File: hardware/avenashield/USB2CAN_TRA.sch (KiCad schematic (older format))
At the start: 29 parts, among them U4 STM32F042C6Tx, U5 MCP2551-I-SN, U9 TXS0102DCT, Y2 16 MHz

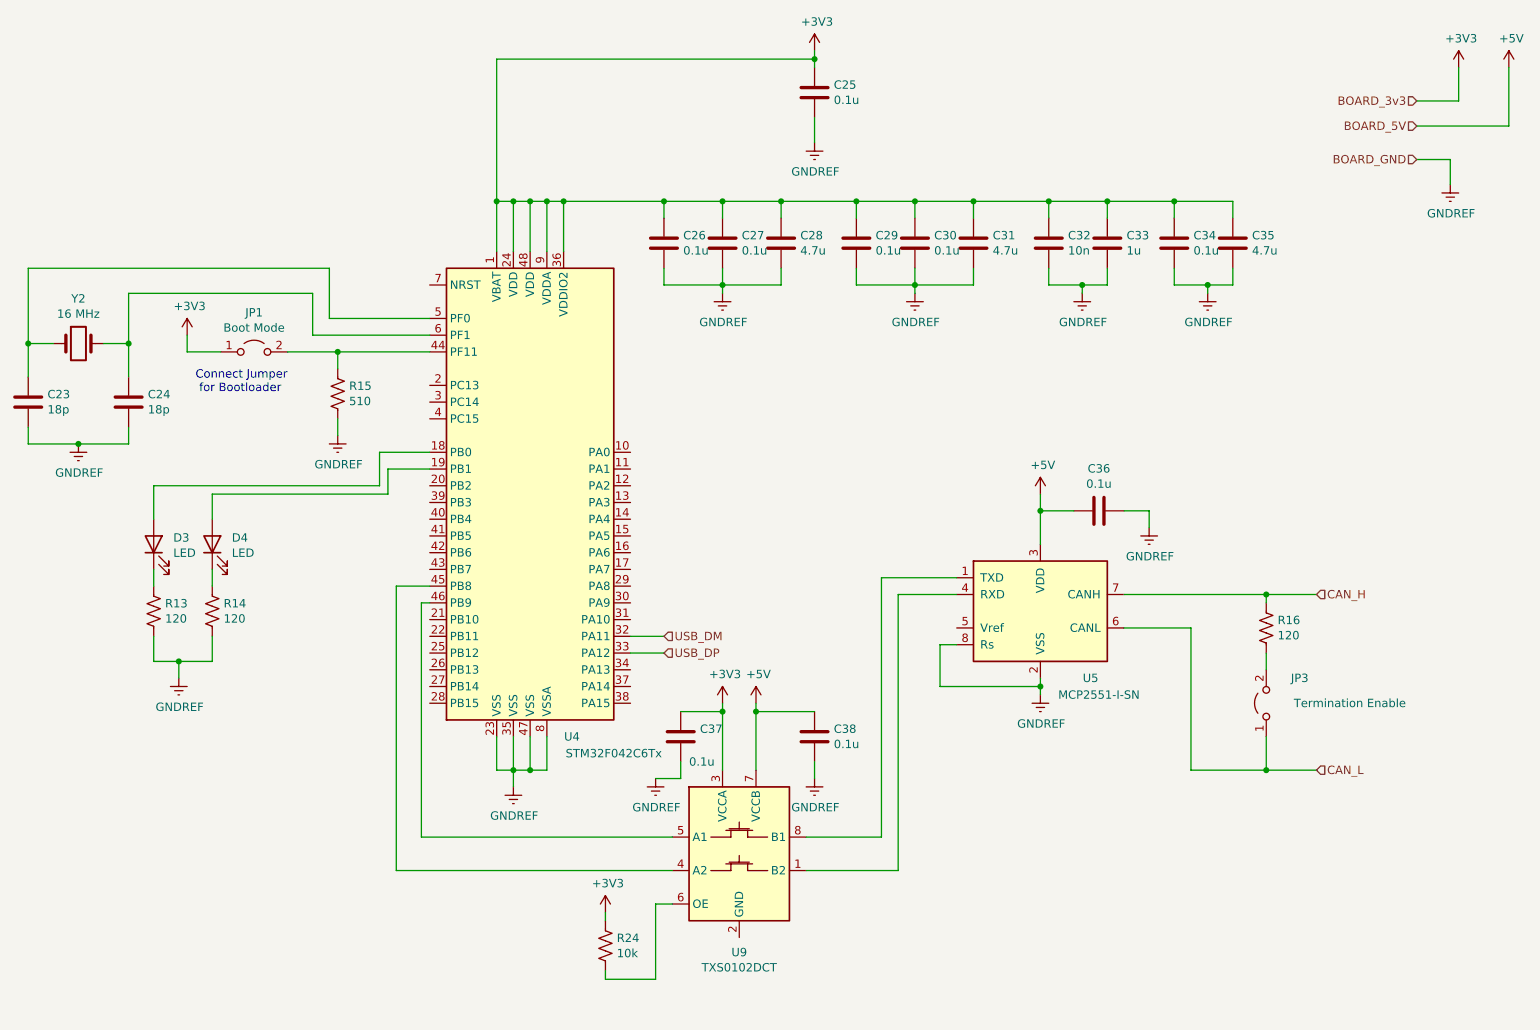
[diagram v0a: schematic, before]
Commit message: Added MiniPCIe latch clip and replaced onboard LEDs with connector
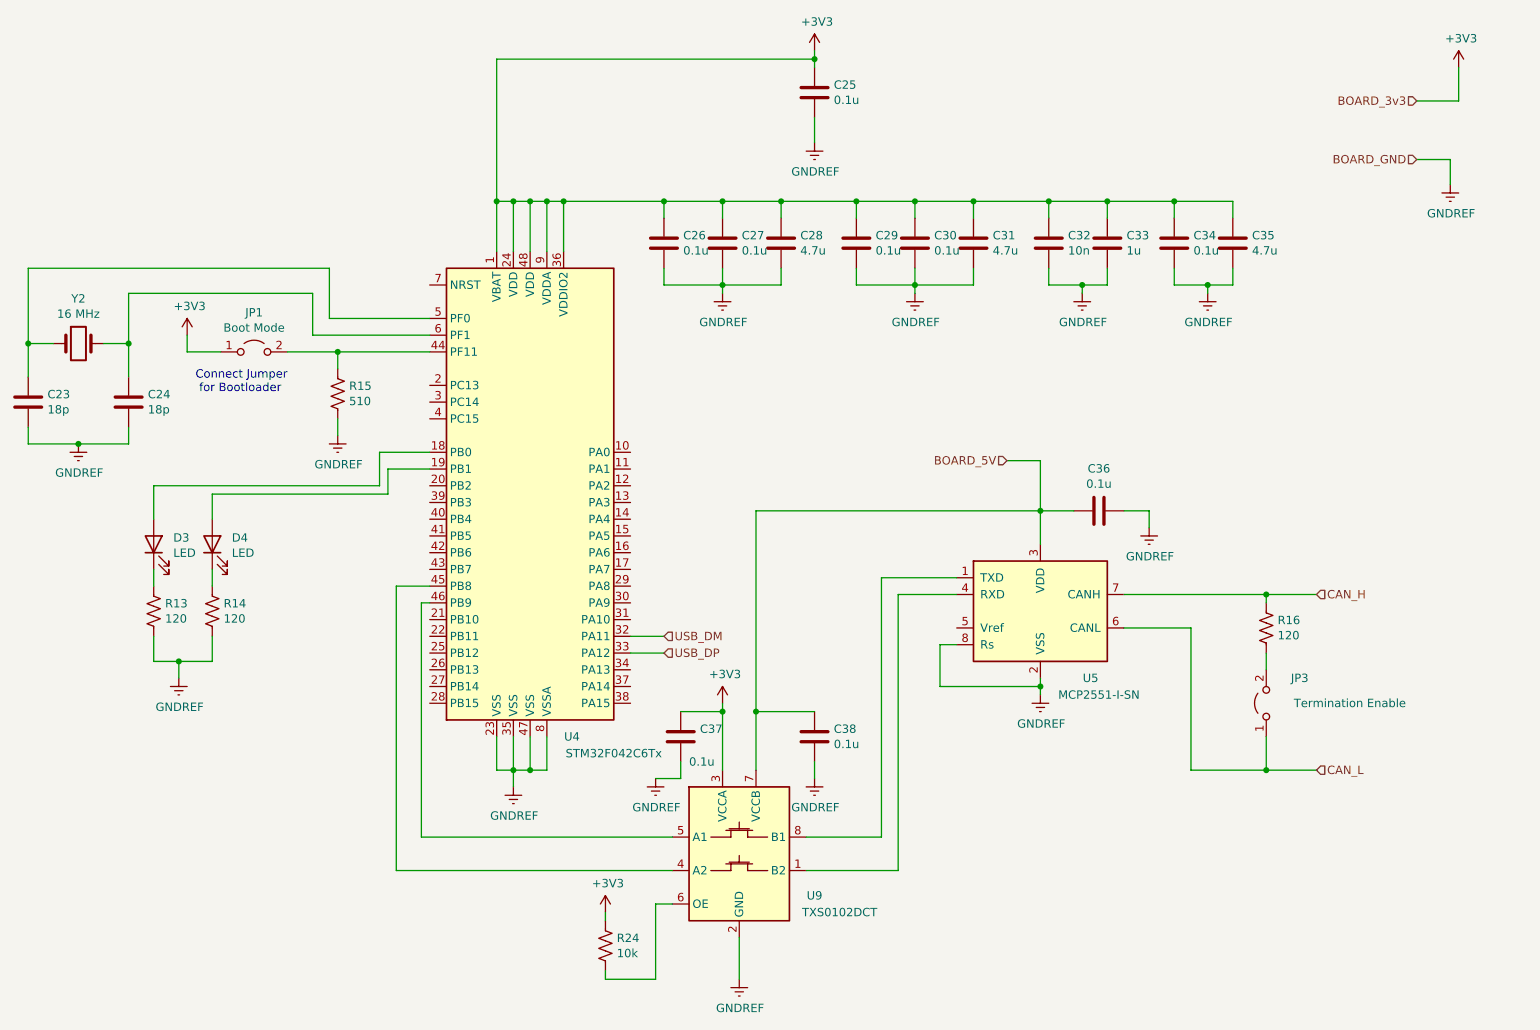
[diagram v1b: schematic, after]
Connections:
- net GNDREF: now also U9.2 (GND)
- net +5V renamed BOARD_5V
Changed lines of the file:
@@
 $EndComp
-$Comp
-L power:+5V #PWR0153
-U 1 1 5E591CA5
-P 7400 3450
-AR Path="/5E564EEA/5E591CA5" Ref="#PWR0153"  Part="1"
-AR Path="/5E45C906/5E591CA5" Ref="#PWR?"  Part="1"
-F 0 "#PWR0153" H 7400 3300 50  0001 C CNN
-F 1 "+5V" H 7415 3623 50  0000 C CNN
-F 2 "" H 7400 3450 50  0001 C CNN
-F 3 "" H 7400 3450 50  0001 C CNN
-	1    7400 3450
-	1    0    0    -1
-$EndComp
-Wire Wire Line
-	7400 3450 7400 3550
 $Comp
 L power:GNDREF #PWR0154
@@
 	1    0    0    -1
 $EndComp
-$Comp
-L power:+5V #PWR0162
-U 1 1 5E61AB69
-P 10200 900
-AR Path="/5E564EEA/5E61AB69" Ref="#PWR0162"  Part="1"
-AR Path="/5E45C906/5E61AB69" Ref="#PWR?"  Part="1"
-F 0 "#PWR0162" H 10200 750 50  0001 C CNN
-F 1 "+5V" H 10215 1073 50  0000 C CNN
-F 2 "" H 10200 900 50  0001 C CNN
-F 3 "" H 10200 900 50  0001 C CNN
-	1    10200 900
-	1    0    0    -1
-$EndComp
 Text HLabel 9650 1100 0    50   Input ~ 0
 BOARD_3v3
-Text HLabel 9650 1250 0    50   Input ~ 0
+Text HLabel 7200 3250 0    50   Input ~ 0
 BOARD_5V
 Wire Wire Line
@@
 Wire Wire Line
 	9900 1100 9900 900
-Wire Wire Line
-	10200 900  10200 1250
-Wire Wire Line
-	10200 1250 9650 1250
 Text HLabel 9650 1450 0    50   Input ~ 0
 BOARD_GND
@@
 U 1 1 5E61F145
 P 5600 5600
-F 0 "U9" H 5600 5011 50  0000 C CNN
-F 1 "TXS0102DCT" H 5600 4920 50  0000 C CNN
+F 0 "U9" H 6050 5350 50  0000 C CNN
+F 1 "TXS0102DCT" H 6200 5250 50  0000 C CNN
 F 2 "Package_SO:SSOP-8_2.95x2.8mm_P0.65mm" H 5600 5050 50  0001 C CNN
 F 3 "http://www.ti.com/lit/gpn/txs0102" H 5600 5580 50  0001 C CNN
@@
 Wire Wire Line
 	3550 4000 3550 5700
-$Comp
-L power:+5V #PWR0140
-U 1 1 5E63CF51
-P 5700 4700
-F 0 "#PWR0140" H 5700 4550 50  0001 C CNN
-F 1 "+5V" H 5715 4873 50  0000 C CNN
-F 2 "" H 5700 4700 50  0001 C CNN
-F 3 "" H 5700 4700 50  0001 C CNN
-	1    5700 4700
-	1    0    0    -1
-$EndComp
 $Comp
 L power:+3V3 #PWR0184
@@
 	1    0    0    -1
 $EndComp
-Wire Wire Line
-	5700 4700 5700 4750
 Wire Wire Line
 	5500 4700 5500 4750
@@
 Wire Wire Line
 	5100 5900 5200 5900
+$Comp
+L power:GNDREF #PWR0195
+U 1 1 5E715CCE
+P 5600 6350
+AR Path="/5E564EEA/5E715CCE" Ref="#PWR0195"  Part="1"
+AR Path="/5E45C906/5E715CCE" Ref="#PWR?"  Part="1"
+F 0 "#PWR0195" H 5600 6100 50  0001 C CNN
+F 1 "GNDREF" H 5605 6177 50  0000 C CNN
+F 2 "" H 5600 6350 50  0001 C CNN
+F 3 "" H 5600 6350 50  0001 C CNN
+	1    5600 6350
+	1    0    0    -1
+$EndComp
+Wire Wire Line
+	5600 6350 5600 6100
+Wire Wire Line
+	7200 3250 7400 3250
+Wire Wire Line
+	7400 3250 7400 3550
+Wire Wire Line
+	5700 3550 7400 3550
+Wire Wire Line
+	5700 3550 5700 4750
 $EndSCHEMATC

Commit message: Changed footprints for CAN connectors and replaced 3D models for headers
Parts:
- C23, C24, C25, C26, C27, C28, C29, C30, C31, C32, C33, C34, C35, C36, C37, C38: footprint Capacitor_SMD:C_0603_1608Metric -> Capacitor_SMD:C_0805_2012Metric_Pad1.15x1.40mm_HandSolder
- R13, R14, R15, R16, R24: footprint Resistor_SMD:R_1206_3216Metric -> Resistor_SMD:R_0805_2012Metric_Pad1.15x1.40mm_HandSolder
- Y2: footprint Crystal:Crystal_SMD_2016-4Pin_2.0x1.6mm -> Crystal:Crystal_SMD_HC49-SD
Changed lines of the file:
@@
 F 0 "C25" H 6165 1096 50  0000 L CNN
 F 1 "0.1u" H 6165 1005 50  0000 L CNN
-F 2 "Capacitor_SMD:C_0603_1608Metric" H 6088 900 50  0001 C CNN
+F 2 "Capacitor_SMD:C_0805_2012Metric_Pad1.15x1.40mm_HandSolder" H 6088 900 50  0001 C CNN
 F 3 "~" H 6050 1050 50  0001 C CNN
 	1    6050 1050
@@
 F 0 "C26" H 5265 1996 50  0000 L CNN
 F 1 "0.1u" H 5265 1905 50  0000 L CNN
-F 2 "Capacitor_SMD:C_0603_1608Metric" H 5188 1800 50  0001 C CNN
+F 2 "Capacitor_SMD:C_0805_2012Metric_Pad1.15x1.40mm_HandSolder" H 5188 1800 50  0001 C CNN
 F 3 "~" H 5150 1950 50  0001 C CNN
 	1    5150 1950
@@
 F 0 "C27" H 5615 1996 50  0000 L CNN
 F 1 "0.1u" H 5615 1905 50  0000 L CNN
-F 2 "Capacitor_SMD:C_0603_1608Metric" H 5538 1800 50  0001 C CNN
+F 2 "Capacitor_SMD:C_0805_2012Metric_Pad1.15x1.40mm_HandSolder" H 5538 1800 50  0001 C CNN
 F 3 "~" H 5500 1950 50  0001 C CNN
 	1    5500 1950
@@
 F 0 "C28" H 5965 1996 50  0000 L CNN
 F 1 "4.7u" H 5965 1905 50  0000 L CNN
-F 2 "Capacitor_SMD:C_0603_1608Metric" H 5888 1800 50  0001 C CNN
+F 2 "Capacitor_SMD:C_0805_2012Metric_Pad1.15x1.40mm_HandSolder" H 5888 1800 50  0001 C CNN
 F 3 "~" H 5850 1950 50  0001 C CNN
 	1    5850 1950
@@
 F 0 "C29" H 6415 1996 50  0000 L CNN
 F 1 "0.1u" H 6415 1905 50  0000 L CNN
-F 2 "Capacitor_SMD:C_0603_1608Metric" H 6338 1800 50  0001 C CNN
+F 2 "Capacitor_SMD:C_0805_2012Metric_Pad1.15x1.40mm_HandSolder" H 6338 1800 50  0001 C CNN
 F 3 "~" H 6300 1950 50  0001 C CNN
 	1    6300 1950
@@
 F 0 "C30" H 6765 1996 50  0000 L CNN
 F 1 "0.1u" H 6765 1905 50  0000 L CNN
-F 2 "Capacitor_SMD:C_0603_1608Metric" H 6688 1800 50  0001 C CNN
+F 2 "Capacitor_SMD:C_0805_2012Metric_Pad1.15x1.40mm_HandSolder" H 6688 1800 50  0001 C CNN
 F 3 "~" H 6650 1950 50  0001 C CNN
 	1    6650 1950
@@
 F 0 "C31" H 7115 1996 50  0000 L CNN
 F 1 "4.7u" H 7115 1905 50  0000 L CNN
-F 2 "Capacitor_SMD:C_0603_1608Metric" H 7038 1800 50  0001 C CNN
+F 2 "Capacitor_SMD:C_0805_2012Metric_Pad1.15x1.40mm_HandSolder" H 7038 1800 50  0001 C CNN
 F 3 "~" H 7000 1950 50  0001 C CNN
 	1    7000 1950
@@
 F 0 "C32" H 7565 1996 50  0000 L CNN
 F 1 "10n" H 7565 1905 50  0000 L CNN
-F 2 "Capacitor_SMD:C_0603_1608Metric" H 7488 1800 50  0001 C CNN
+F 2 "Capacitor_SMD:C_0805_2012Metric_Pad1.15x1.40mm_HandSolder" H 7488 1800 50  0001 C CNN
 F 3 "~" H 7450 1950 50  0001 C CNN
 	1    7450 1950
@@
 F 0 "C33" H 7915 1996 50  0000 L CNN
 F 1 "1u" H 7915 1905 50  0000 L CNN
-F 2 "Capacitor_SMD:C_0603_1608Metric" H 7838 1800 50  0001 C CNN
+F 2 "Capacitor_SMD:C_0805_2012Metric_Pad1.15x1.40mm_HandSolder" H 7838 1800 50  0001 C CNN
 F 3 "~" H 7800 1950 50  0001 C CNN
 	1    7800 1950
@@
 F 0 "C34" H 8315 1996 50  0000 L CNN
 F 1 "0.1u" H 8315 1905 50  0000 L CNN
-F 2 "Capacitor_SMD:C_0603_1608Metric" H 8238 1800 50  0001 C CNN
+F 2 "Capacitor_SMD:C_0805_2012Metric_Pad1.15x1.40mm_HandSolder" H 8238 1800 50  0001 C CNN
 F 3 "~" H 8200 1950 50  0001 C CNN
 	1    8200 1950
@@
 F 0 "C35" H 8665 1996 50  0000 L CNN
 F 1 "4.7u" H 8665 1905 50  0000 L CNN
-F 2 "Capacitor_SMD:C_0603_1608Metric" H 8588 1800 50  0001 C CNN
+F 2 "Capacitor_SMD:C_0805_2012Metric_Pad1.15x1.40mm_HandSolder" H 8588 1800 50  0001 C CNN
 F 3 "~" H 8550 1950 50  0001 C CNN
 	1    8550 1950
@@
 F 0 "C36" V 7498 3550 50  0000 C CNN
 F 1 "0.1u" V 7589 3550 50  0000 C CNN
-F 2 "Capacitor_SMD:C_0603_1608Metric" H 7788 3400 50  0001 C CNN
+F 2 "Capacitor_SMD:C_0805_2012Metric_Pad1.15x1.40mm_HandSolder" H 7788 3400 50  0001 C CNN
 F 3 "~" H 7750 3550 50  0001 C CNN
 	1    7750 3550
@@
 F 0 "R15" H 3268 2896 50  0000 L CNN
 F 1 "510" H 3268 2805 50  0000 L CNN
-F 2 "Resistor_SMD:R_1206_3216Metric" V 3240 2840 50  0001 C CNN
+F 2 "Resistor_SMD:R_0805_2012Metric_Pad1.15x1.40mm_HandSolder" V 3240 2840 50  0001 C CNN
 F 3 "~" H 3200 2850 50  0001 C CNN
 	1    3200 2850
@@
 F 0 "C24" H 2065 2946 50  0000 L CNN
 F 1 "18p" H 2065 2855 50  0000 L CNN
-F 2 "Capacitor_SMD:C_0603_1608Metric" H 1988 2750 50  0001 C CNN
+F 2 "Capacitor_SMD:C_0805_2012Metric_Pad1.15x1.40mm_HandSolder" H 1988 2750 50  0001 C CNN
 F 3 "~" H 1950 2900 50  0001 C CNN
 	1    1950 2900
@@
 F 0 "Y2" H 1650 2818 50  0000 C CNN
 F 1 "16 MHz" H 1650 2727 50  0000 C CNN
-F 2 "Crystal:Crystal_SMD_2016-4Pin_2.0x1.6mm" H 1650 2550 50  0001 C CNN
+F 2 "Crystal:Crystal_SMD_HC49-SD" H 1650 2550 50  0001 C CNN
 F 3 "~" H 1650 2550 50  0001 C CNN
 	1    1650 2550
@@
 F 0 "C23" H 1465 2946 50  0000 L CNN
 F 1 "18p" H 1465 2855 50  0000 L CNN
-F 2 "Capacitor_SMD:C_0603_1608Metric" H 1388 2750 50  0001 C CNN
+F 2 "Capacitor_SMD:C_0805_2012Metric_Pad1.15x1.40mm_HandSolder" H 1388 2750 50  0001 C CNN
 F 3 "~" H 1350 2900 50  0001 C CNN
 	1    1350 2900
@@
 F 0 "R13" H 2168 4196 50  0000 L CNN
 F 1 "120" H 2168 4105 50  0000 L CNN
-F 2 "Resistor_SMD:R_1206_3216Metric" V 2140 4140 50  0001 C CNN
+F 2 "Resistor_SMD:R_0805_2012Metric_Pad1.15x1.40mm_HandSolder" V 2140 4140 50  0001 C CNN
 F 3 "~" H 2100 4150 50  0001 C CNN
 	1    2100 4150
@@
 F 0 "R14" H 2518 4196 50  0000 L CNN
 F 1 "120" H 2518 4105 50  0000 L CNN
-F 2 "Resistor_SMD:R_1206_3216Metric" V 2490 4140 50  0001 C CNN
+F 2 "Resistor_SMD:R_0805_2012Metric_Pad1.15x1.40mm_HandSolder" V 2490 4140 50  0001 C CNN
 F 3 "~" H 2450 4150 50  0001 C CNN
 	1    2450 4150
@@
 F 0 "R16" H 8818 4296 50  0000 L CNN
 F 1 "120" H 8818 4205 50  0000 L CNN
-F 2 "Resistor_SMD:R_1206_3216Metric" V 8790 4240 50  0001 C CNN
+F 2 "Resistor_SMD:R_0805_2012Metric_Pad1.15x1.40mm_HandSolder" V 8790 4240 50  0001 C CNN
 F 3 "~" H 8750 4250 50  0001 C CNN
 	1    8750 4250
@@
 F 0 "C38" H 6165 4946 50  0000 L CNN
 F 1 "0.1u" H 6165 4855 50  0000 L CNN
-F 2 "Capacitor_SMD:C_0603_1608Metric" H 6088 4750 50  0001 C CNN
+F 2 "Capacitor_SMD:C_0805_2012Metric_Pad1.15x1.40mm_HandSolder" H 6088 4750 50  0001 C CNN
 F 3 "~" H 6050 4900 50  0001 C CNN
 	1    6050 4900
@@
 F 0 "C37" H 5365 4946 50  0000 L CNN
 F 1 "0.1u" H 5300 4750 50  0000 L CNN
-F 2 "Capacitor_SMD:C_0603_1608Metric" H 5288 4750 50  0001 C CNN
+F 2 "Capacitor_SMD:C_0805_2012Metric_Pad1.15x1.40mm_HandSolder" H 5288 4750 50  0001 C CNN
 F 3 "~" H 5250 4900 50  0001 C CNN
 	1    5250 4900
@@
 F 0 "R24" H 4732 6104 50  0000 R CNN
 F 1 "10k" H 4732 6195 50  0000 R CNN
-F 2 "Resistor_SMD:R_1206_3216Metric" V 4840 6140 50  0001 C CNN
+F 2 "Resistor_SMD:R_0805_2012Metric_Pad1.15x1.40mm_HandSolder" V 4840 6140 50  0001 C CNN
 F 3 "~" H 4800 6150 50  0001 C CNN
 	1    4800 6150
